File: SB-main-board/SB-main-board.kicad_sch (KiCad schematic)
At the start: 92 parts, among them J1 XT30PB_IN, J2 USB_C_Receptacle_USB2.0_16P, J3 Excluder, J4 PT100, J5 Hotend, J6 FAN2, J7 LDC, J8 FS, J9 FAN, Q1 BUK9M8R5-40EX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

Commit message: mechanical: fix interference
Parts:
- J6, J8: footprint Library:JST_PH_B4B-PH-SM4-TB_1x04-1MP_P2.00mm_Vertical -> Connector_Molex:Molex_PicoBlade_53398-0471_1x04-1MP_P1.25mm_Vertical
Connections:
- net +24V: now also J6.4 (Pin_4); no longer J6.1 (Pin_1)
- net +3V3B: now also J8.4 (Pin_4); no longer J8.1 (Pin_1)
- net ENDSTOP0: now also J8.3 (Pin_3); no longer J8.2 (Pin_2)
- net FAN2_DET: now also J6.2 (Pin_2); no longer J6.3 (Pin_3)
- net FAN2_PWM: now also J6.3 (Pin_3); no longer J6.2 (Pin_2)
- net FS: now also J8.2 (Pin_2); no longer J8.3 (Pin_3)
- net GND: now also J6.1 (Pin_1), J8.1 (Pin_1); no longer J6.4 (Pin_4), J8.4 (Pin_4)

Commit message: silkscreen: optmise silkscreen
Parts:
- J6, J8: footprint Connector_Molex:Molex_PicoBlade_53398-0471_1x04-1MP_P1.25mm_Vertical -> Library:Molex_PicoBlade_53398-0471_1x04-1MP_P1.25mm_Vertical
- J9: footprint Connector_PinHeader_2.00mm:PinHeader_2x06_P2.00mm_Horizontal -> Library:PinHeader_2x06_P2.00mm_Horizontal
- L1: footprint Inductor_SMD:L_Chilisin_BMRA00040420 -> Inductor_SMD:L_Sunlord_SWPA4030S
- Y1: footprint Crystal:Crystal_SMD_2016-4Pin_2.0x1.6mm -> Crystal:Crystal_SMD_2520-4Pin_2.5x2.0mm
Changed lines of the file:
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@@
 			)
 		)
-		(property "Footprint" "Connector_Molex:Molex_PicoBlade_53398-0471_1x04-1MP_P1.25mm_Vertical"
+		(property "Footprint" "Library:Molex_PicoBlade_53398-0471_1x04-1MP_P1.25mm_Vertical"
 			(at 278.13 115.57 0)
 			(effects
@@
 			)
 		)
-		(property "Footprint" "Inductor_SMD:L_Chilisin_BMRA00040420"
+		(property "Footprint" "Inductor_SMD:L_Sunlord_SWPA4030S"
 			(at 80.01 260.35 0)
 			(effects
@@
 			)
 		)
-		(property "Footprint" "Connector_Molex:Molex_PicoBlade_53398-0471_1x04-1MP_P1.25mm_Vertical"
+		(property "Footprint" "Library:Molex_PicoBlade_53398-0471_1x04-1MP_P1.25mm_Vertical"
 			(at 278.13 67.31 0)
 			(effects
@@
 			)
 		)
-		(property "Footprint" "Connector_PinHeader_2.00mm:PinHeader_2x06_P2.00mm_Horizontal"
+		(property "Footprint" "Library:PinHeader_2x06_P2.00mm_Horizontal"
 			(at 271.78 146.05 0)
 			(effects
@@
 			)
 		)
-		(property "Footprint" "Crystal:Crystal_SMD_2016-4Pin_2.0x1.6mm"
+		(property "Footprint" "Crystal:Crystal_SMD_2520-4Pin_2.5x2.0mm"
 			(at 40.64 109.22 0)
 			(effects

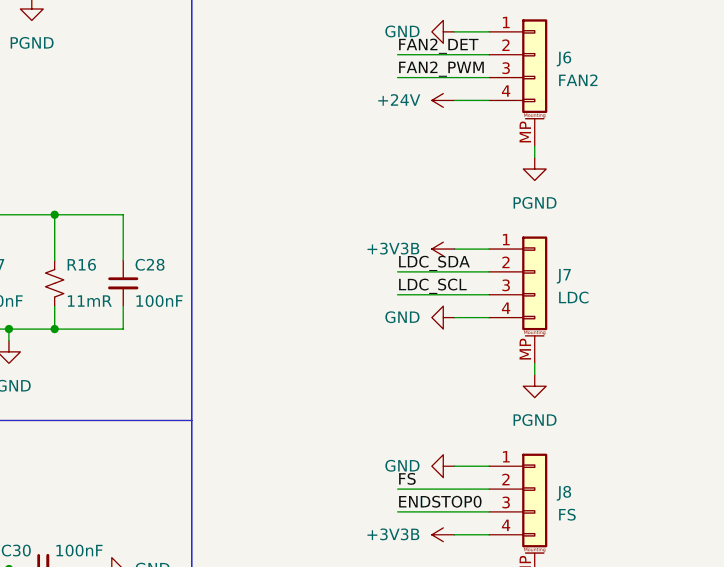
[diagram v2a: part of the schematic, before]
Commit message: bugfix: use 5V for IDM sensor
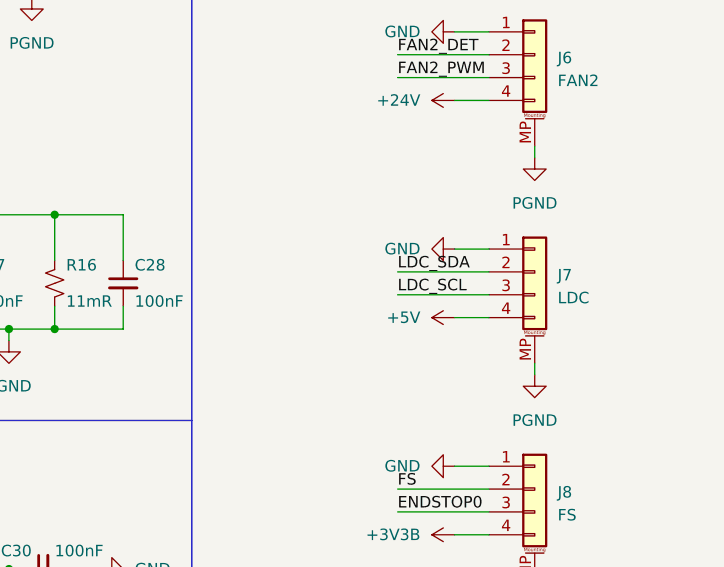
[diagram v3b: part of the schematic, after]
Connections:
- net +3V3B: no longer J7.1 (Pin_1)
- net +5V: now also J7.4 (Pin_4)
- net GND: now also J7.1 (Pin_1); no longer J7.4 (Pin_4)
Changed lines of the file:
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@@
-	)
-	(symbol
-		(lib_id "power:+3V3")
-		(at 269.24 88.9 90)
-		(unit 1)
-		(exclude_from_sim no)
-		(in_bom yes)
-		(on_board yes)
-		(dnp no)
-		(fields_autoplaced yes)
-		(property "Reference" "#PWR0163"
-			(at 273.05 88.9 0)
-			(effects
-				(font
-					(size 1.27 1.27)
-				)
-				(hide yes)
-			)
-		)
-		(property "Value" "+3V3B"
-			(at 265.43 88.8999 90)
-			(effects
-				(font
-					(size 1.27 1.27)
-				)
-				(justify left)
-			)
-		)
-		(property "Footprint" ""
-			(at 269.24 88.9 0)
-			(effects
-				(font
-					(size 1.27 1.27)
-				)
-				(hide yes)
-			)
-		)
-		(property "Datasheet" ""
-			(at 269.24 88.9 0)
-			(effects
-				(font
-					(size 1.27 1.27)
-				)
-				(hide yes)
-			)
-		)
-		(property "Description" "Power symbol creates a global label with name \"+3V3\""
-			(at 269.24 88.9 0)
-			(effects
-				(font
-					(size 1.27 1.27)
-				)
-				(hide yes)
-			)
-		)
-		(pin "1"
-		)
-		(instances
-			(project "SB-main-board"
-				(path "/e3d9bf3f-f8be-4a0d-9b69-f1016d65a8ba"
-					(reference "#PWR0163")
-					(unit 1)
-				)
-			)
-		)
 	)
 	(symbol
@@
 	(symbol
 		(lib_id "power:GND")
-		(at 269.24 96.52 270)
+		(at 269.24 88.9 270)
+		(mirror x)
 		(unit 1)
 		(exclude_from_sim no)
@@
 		(fields_autoplaced yes)
 		(property "Reference" "#PWR0164"
-			(at 262.89 96.52 0)
+			(at 262.89 88.9 0)
 			(effects
 				(font
@@
 		)
 		(property "Value" "GND"
-			(at 265.43 96.5199 90)
+			(at 265.43 88.9001 90)
 			(effects
 				(font
@@
 		)
 		(property "Footprint" ""
-			(at 269.24 96.52 0)
+			(at 269.24 88.9 0)
 			(effects
 				(font
@@
 		)
 		(property "Datasheet" ""
-			(at 269.24 96.52 0)
+			(at 269.24 88.9 0)
 			(effects
 				(font
@@
 		)
 		(property "Description" "Power symbol creates a global label with name \"GND\" , ground"
-			(at 269.24 96.52 0)
+			(at 269.24 88.9 0)
 			(effects
 				(font
@@
 					(unit 1)
 				)
+			)
+		)
+	)
+	(symbol
+		(lib_id "power:+5V")
+		(at 269.24 96.52 90)
+		(unit 1)
+		(exclude_from_sim no)
+		(in_bom yes)
+		(on_board yes)
+		(dnp no)
+		(fields_autoplaced yes)
+		(property "Reference" "#PWR018"
+			(at 273.05 96.52 0)
+			(effects
+				(font
+					(size 1.27 1.27)
+				)
+				(hide yes)
+			)
+		)
+		(property "Value" "+5V"
+			(at 265.43 96.5199 90)
+			(effects
+				(font
+					(size 1.27 1.27)
+				)
+				(justify left)
+			)
+		)
+		(property "Footprint" ""
+			(at 269.24 96.52 0)
+			(effects
+				(font
+					(size 1.27 1.27)
+				)
+				(hide yes)
+			)
+		)
+		(property "Datasheet" ""
+			(at 269.24 96.52 0)
+			(effects
+				(font
+					(size 1.27 1.27)
+				)
+				(hide yes)
+			)
+		)
+		(property "Description" "Power symbol creates a global label with name \"+5V\""
+			(at 269.24 96.52 0)
+			(effects
+				(font
+					(size 1.27 1.27)
+				)
+				(hide yes)
+			)
+		)
+		(pin "1"
+		)
+		(instances
+			(project "SB-main-board"
+				(path "/e3d9bf3f-f8be-4a0d-9b69-f1016d65a8ba"
+					(reference "#PWR018")
+					(unit 1)
+				)

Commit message: fab: generate gerbers and bom
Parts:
- R2, R4: now not fitted
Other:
- company: (none) -> Lassi-Cat
- title: (none) -> StealthBurner CAN Main
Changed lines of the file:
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@@
 	(generator_version "8.0")
 	(paper "A3")
+	(title_block
+		(title "StealthBurner CAN Main")
+		(date "2024-06-02")
+		(rev "A0")
+		(company "Lassi-Cat")
+		(comment 1 "Author: Charlie Yu")
+		(comment 4 "CAN toolhead board for StealthBurner")
+	)
 	(junction
 		(at 71.12 234.95)
@@
 		(in_bom yes)
 		(on_board yes)
-		(dnp no)
+		(dnp yes)
 		(property "Reference" "R4"
 			(at 39.37 92.71 90)
@@
 		(in_bom yes)
 		(on_board yes)
-		(dnp no)
+		(dnp yes)
 		(property "Reference" "R2"
 			(at 21.59 44.45 90)

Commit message: generate gerber files
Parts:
- removed J4: PT100, Library:Molex_PicoBlade_53261-0371_1x03-1MP_P1.25mm_Horizontal, symbol Connector_Generic_MountingPin:Conn_01x03_MountingPin
- added J4: PT100, Library:Molex_PicoBlade_53261-0471_1x04-1MP_P1.25mm_Horizontal, symbol Connector_Generic_MountingPin:Conn_01x04_MountingPin
- added S1: Select, Library:Select, symbol Connector_Generic:Conn_01x03
- R11: now not fitted
- R17: footprint Resistor_SMD:R_0402_1005Metric -> Resistor_SMD:R_0603_1608Metric
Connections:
- net GND: now also J4.MP (MountPin), S1.1 (Pin_1)
- net at U9.5 (FORCE+): now also J4.4 (Pin_4), S1.3 (Pin_3); no longer U9.6 (FORCE2)
- net at C33.1, U9.7 (RTDIN+): now also J4.3 (Pin_3)
- net at C33.2, U9.8 (RTDIN-): now also J4.2 (Pin_2); no longer U9.9 (FORCE-)
- new net: S1.2 (Pin_2), U9.6 (FORCE2)
- new net: J4.1 (Pin_1), U9.9 (FORCE-)

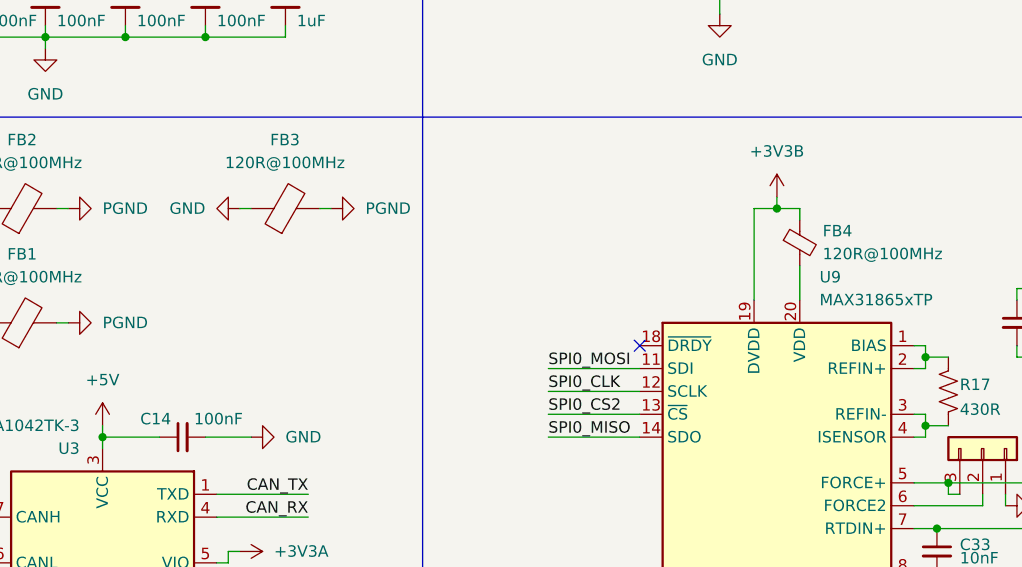
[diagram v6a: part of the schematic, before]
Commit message: sch: optimize return path
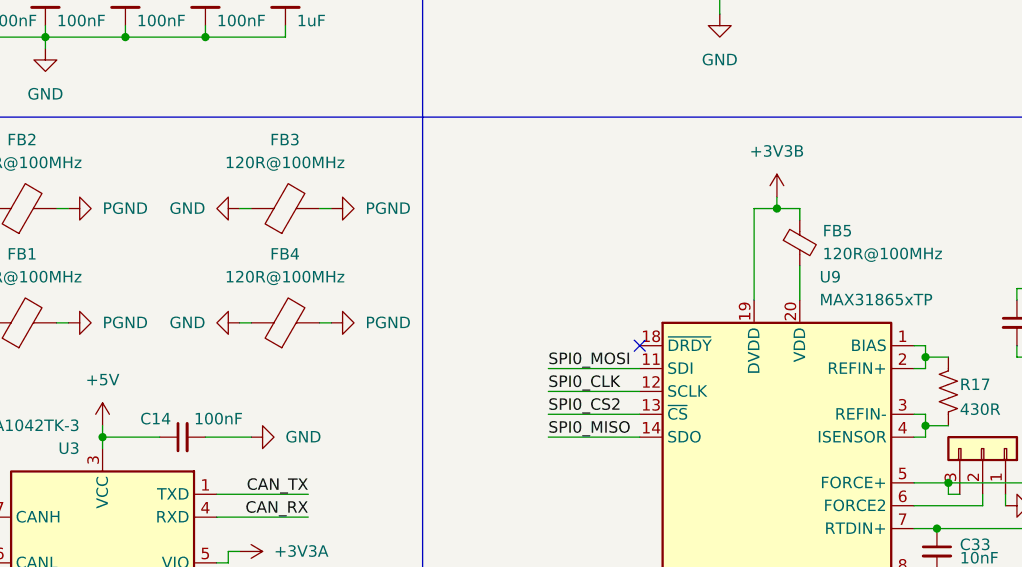
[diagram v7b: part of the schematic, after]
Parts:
- added FB4: 120R@100MHz, Inductor_SMD:L_0603_1608Metric, symbol Device:FerriteBead
- renumbered FB4 to FB5
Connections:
- net GND: now also FB4.1
- net PGND: now also FB4.2
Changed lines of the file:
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@@
 	(wire
 		(pts
+			(xy 124.46 186.69) (xy 125.73 186.69)
+		)
+		(stroke
+			(width 0)
+			(type default)
+		)
+	)
+	(wire
+		(pts
 			(xy 264.16 24.13) (xy 262.89 24.13)
 		)
@@
 	(wire
 		(pts
+			(xy 133.35 186.69) (xy 134.62 186.69)
+		)
+		(stroke
+			(width 0)
+			(type default)
+		)
+	)
+	(wire
+		(pts
 			(xy 57.15 208.28) (xy 58.42 208.28)
 		)
@@
 		(dnp no)
 		(fields_autoplaced yes)
-		(property "Reference" "FB4"
+		(property "Reference" "FB5"
 			(at 189.23 176.4918 0)
 			(effects
@@
 			(project "SB-main-board"
 				(path "/e3d9bf3f-f8be-4a0d-9b69-f1016d65a8ba"
-					(reference "FB4")
+					(reference "FB5")
 					(unit 1)
 				)
@@
 	)
 	(symbol
+		(lib_id "Device:FerriteBead")
+		(at 129.54 186.69 90)
+		(unit 1)
+		(exclude_from_sim no)
+		(in_bom yes)
+		(on_board yes)
+		(dnp no)
+		(property "Reference" "FB4"
+			(at 129.4892 179.07 90)
+			(effects
+				(font
+					(size 1.27 1.27)
+				)
+			)
+		)
+		(property "Value" "120R@100MHz"
+			(at 129.4892 181.61 90)
+			(effects
+				(font
+					(size 1.27 1.27)
+				)
+			)
+		)
+		(property "Footprint" "Inductor_SMD:L_0603_1608Metric"
+			(at 129.54 188.468 90)
+			(effects
+				(font
+					(size 1.27 1.27)
+				)
+				(hide yes)
+			)
+		)
+		(property "Datasheet" "~"
+			(at 129.54 186.69 0)
+			(effects
+				(font
+					(size 1.27 1.27)
+				)
+				(hide yes)
+			)
+		)
+		(property "Description" "Ferrite bead"
+			(at 129.54 186.69 0)
+			(effects
+				(font
+					(size 1.27 1.27)
+				)
+				(hide yes)
+			)
+		)
+		(pin "2"
+		)
+		(pin "1"
+		)
+		(instances
+			(project "SB-main-board"
+				(path "/e3d9bf3f-f8be-4a0d-9b69-f1016d65a8ba"
+					(reference "FB4")
+					(unit 1)
+				)
+			)
+		)
+	)
+	(symbol
 		(lib_id "power:GND")
 		(at 27.94 85.09 0)
@@
 	(symbol
 		(lib_id "power:GND")
+		(at 124.46 186.69 270)
+		(unit 1)
+		(exclude_from_sim no)
+		(in_bom yes)
+		(on_board yes)
+		(dnp no)
+		(fields_autoplaced yes)
+		(property "Reference" "#PWR020"
+			(at 118.11 186.69 0)
+			(effects
+				(font
+					(size 1.27 1.27)
+				)
+				(hide yes)
+			)
+		)
+		(property "Value" "GND"
+			(at 120.65 186.6899 90)
+			(effects
+				(font
+					(size 1.27 1.27)
+				)
+				(justify right)
+			)
+		)
+		(property "Footprint" ""
+			(at 124.46 186.69 0)
+			(effects
+				(font
+					(size 1.27 1.27)
+				)
+				(hide yes)
+			)
+		)
+		(property "Datasheet" ""
+			(at 124.46 186.69 0)
+			(effects
+				(font
+					(size 1.27 1.27)
+				)
+				(hide yes)
+			)
+		)
+		(property "Description" "Power symbol creates a global label with name \"GND\" , ground"
+			(at 124.46 186.69 0)
+			(effects
+				(font
+					(size 1.27 1.27)
+				)
+				(hide yes)
+			)
+		)
+		(pin "1"
+		)
+		(instances
+			(project "SB-main-board"
+				(path "/e3d9bf3f-f8be-4a0d-9b69-f1016d65a8ba"
+					(reference "#PWR020")
+					(unit 1)
+				)
+			)
+		)
+	)
+	(symbol
+		(lib_id "power:GND")
 		(at 215.9 191.77 0)
 		(unit 1)
@@
 					(unit 1)
 				)
+			)
+		)
+	)
+	(symbol
+		(lib_id "power:GND")
+		(at 134.62 186.69 90)
+		(unit 1)
+		(exclude_from_sim no)
+		(in_bom yes)
+		(on_board yes)
+		(dnp no)
+		(fields_autoplaced yes)
+		(property "Reference" "#PWR021"
+			(at 140.97 186.69 0)
+			(effects
+				(font
+					(size 1.27 1.27)
+				)
+				(hide yes)
+			)
+		)
+		(property "Value" "PGND"
+			(at 138.43 186.6899 90)
+			(effects
+				(font
+					(size 1.27 1.27)
+				)
+				(justify right)
+			)
+		)
+		(property "Footprint" ""
+			(at 134.62 186.69 0)
+			(effects
+				(font
+					(size 1.27 1.27)
+				)
+				(hide yes)
+			)
+		)
+		(property "Datasheet" ""
+			(at 134.62 186.69 0)
+			(effects
+				(font
+					(size 1.27 1.27)
+				)
+				(hide yes)
+			)
+		)
+		(property "Description" "Power symbol creates a global label with name \"GND\" , ground"
+			(at 134.62 186.69 0)
+			(effects
+				(font
+					(size 1.27 1.27)
+				)
+				(hide yes)
+			)
+		)
+		(pin "1"
+		)
+		(instances
+			(project "SB-main-board"
+				(path "/e3d9bf3f-f8be-4a0d-9b69-f1016d65a8ba"
+					(reference "#PWR021")
+					(unit 1)
+				)

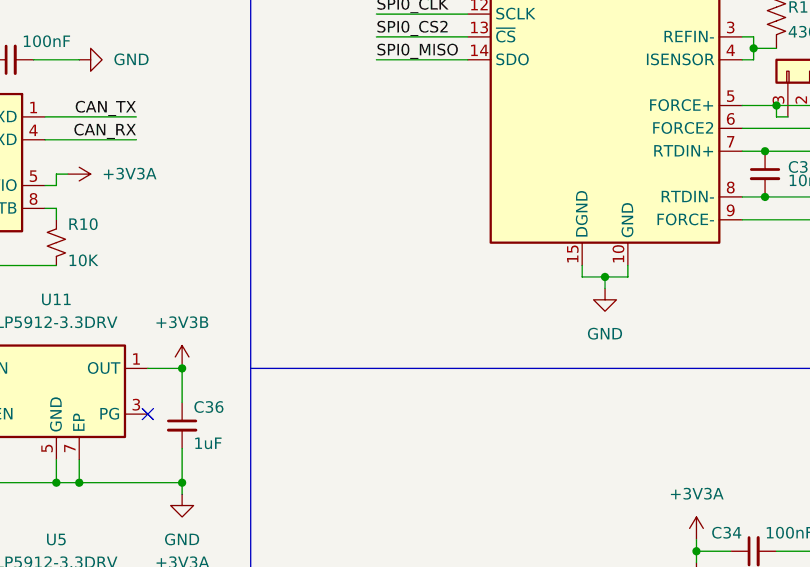
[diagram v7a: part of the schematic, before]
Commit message: layout: optmise power layout
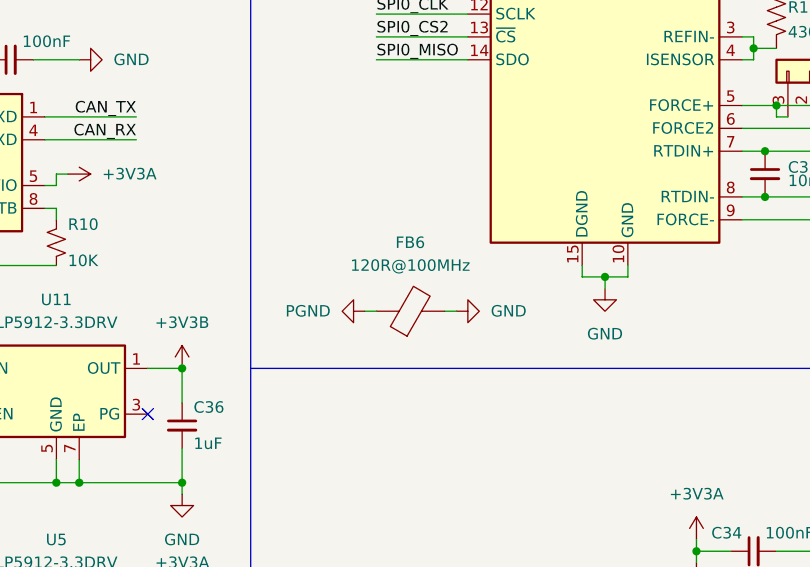
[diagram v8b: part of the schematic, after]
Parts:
- added FB6: 120R@100MHz, Inductor_SMD:L_0603_1608Metric, symbol Device:FerriteBead
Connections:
- net GND: now also FB6.2
- net PGND: now also FB6.1
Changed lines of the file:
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@@
 	(wire
 		(pts
+			(xy 157.48 227.33) (xy 158.75 227.33)
+		)
+		(stroke
+			(width 0)
+			(type default)
+		)
+	)
+	(wire
+		(pts
 			(xy 152.4 140.97) (xy 162.56 140.97)
 		)
@@
 	(wire
 		(pts
+			(xy 166.37 227.33) (xy 167.64 227.33)
+		)
+		(stroke
+			(width 0)
+			(type default)
+		)
+	)
+	(wire
+		(pts
 			(xy 27.94 67.31) (xy 27.94 68.58)
 		)
@@
 	)
 	(symbol
+		(lib_id "power:GND")
+		(at 167.64 227.33 90)
+		(mirror x)
+		(unit 1)
+		(exclude_from_sim no)
+		(in_bom yes)
+		(on_board yes)
+		(dnp no)
+		(fields_autoplaced yes)
+		(property "Reference" "#PWR022"
+			(at 173.99 227.33 0)
+			(effects
+				(font
+					(size 1.27 1.27)
+				)
+				(hide yes)
+			)
+		)
+		(property "Value" "GND"
+			(at 171.45 227.3299 90)
+			(effects
+				(font
+					(size 1.27 1.27)
+				)
+				(justify right)
+			)
+		)
+		(property "Footprint" ""
+			(at 167.64 227.33 0)
+			(effects
+				(font
+					(size 1.27 1.27)
+				)
+				(hide yes)
+			)
+		)
+		(property "Datasheet" ""
+			(at 167.64 227.33 0)
+			(effects
+				(font
+					(size 1.27 1.27)
+				)
+				(hide yes)
+			)
+		)
+		(property "Description" "Power symbol creates a global label with name \"GND\" , ground"
+			(at 167.64 227.33 0)
+			(effects
+				(font
+					(size 1.27 1.27)
+				)
+				(hide yes)
+			)
+		)
+		(pin "1"
+		)
+		(instances
+			(project "SB-main-board"
+				(path "/e3d9bf3f-f8be-4a0d-9b69-f1016d65a8ba"
+					(reference "#PWR022")
+					(unit 1)
+				)
+			)
+		)
+	)
+	(symbol
 		(lib_id "Sensor_Temperature:MAX31865xTP")
 		(at 184.15 204.47 0)
@@
 	)
 	(symbol
+		(lib_id "Device:FerriteBead")
+		(at 162.56 227.33 90)
+		(unit 1)
+		(exclude_from_sim no)
+		(in_bom yes)
+		(on_board yes)
+		(dnp no)
+		(property "Reference" "FB6"
+			(at 162.5092 219.71 90)
+			(effects
+				(font
+					(size 1.27 1.27)
+				)
+			)
+		)
+		(property "Value" "120R@100MHz"
+			(at 162.5092 222.25 90)
+			(effects
+				(font
+					(size 1.27 1.27)
+				)
+			)
+		)
+		(property "Footprint" "Inductor_SMD:L_0603_1608Metric"
+			(at 162.56 229.108 90)
+			(effects
+				(font
+					(size 1.27 1.27)
+				)
+				(hide yes)
+			)
+		)
+		(property "Datasheet" "~"
+			(at 162.56 227.33 0)
+			(effects
+				(font
+					(size 1.27 1.27)
+				)
+				(hide yes)
+			)
+		)
+		(property "Description" "Ferrite bead"
+			(at 162.56 227.33 0)
+			(effects
+				(font
+					(size 1.27 1.27)
+				)
+				(hide yes)
+			)
+		)
+		(pin "2"
+		)
+		(pin "1"
+		)
+		(instances
+			(project "SB-main-board"
+				(path "/e3d9bf3f-f8be-4a0d-9b69-f1016d65a8ba"
+					(reference "FB6")
+					(unit 1)
+				)
+			)
+		)
+	)
+	(symbol
 		(lib_id "power:+1V1")
 		(at 87.63 127 0)
@@
 					(unit 1)
 				)
+			)
+		)
+	)
+	(symbol
+		(lib_id "power:GND")
+		(at 157.48 227.33 270)
+		(mirror x)
+		(unit 1)
+		(exclude_from_sim no)
+		(in_bom yes)
+		(on_board yes)
+		(dnp no)
+		(fields_autoplaced yes)
+		(property "Reference" "#PWR023"
+			(at 151.13 227.33 0)
+			(effects
+				(font
+					(size 1.27 1.27)
+				)
+				(hide yes)
+			)
+		)
+		(property "Value" "PGND"
+			(at 153.67 227.3299 90)
+			(effects
+				(font
+					(size 1.27 1.27)
+				)
+				(justify right)
+			)
+		)
+		(property "Footprint" ""
+			(at 157.48 227.33 0)
+			(effects
+				(font
+					(size 1.27 1.27)
+				)
+				(hide yes)
+			)
+		)
+		(property "Datasheet" ""
+			(at 157.48 227.33 0)
+			(effects
+				(font
+					(size 1.27 1.27)
+				)
+				(hide yes)
+			)
+		)
+		(property "Description" "Power symbol creates a global label with name \"GND\" , ground"
+			(at 157.48 227.33 0)
+			(effects
+				(font
+					(size 1.27 1.27)
+				)
+				(hide yes)
+			)
+		)
+		(pin "1"
+		)
+		(instances
+			(project "SB-main-board"
+				(path "/e3d9bf3f-f8be-4a0d-9b69-f1016d65a8ba"
+					(reference "#PWR023")
+					(unit 1)
+				)
